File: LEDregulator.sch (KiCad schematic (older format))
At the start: 43 parts, among them J1 2.1mm DC jack, J2 2way Screw Terminal, J3 2way Screw Terminal, J4 2way Screw Terminal, J5 2way Screw Terminal, J6 2way Screw Terminal, J7 2way Screw Terminal, Q1 BSS138W, SW1 DPDT Switch, SW2 6pos rotary

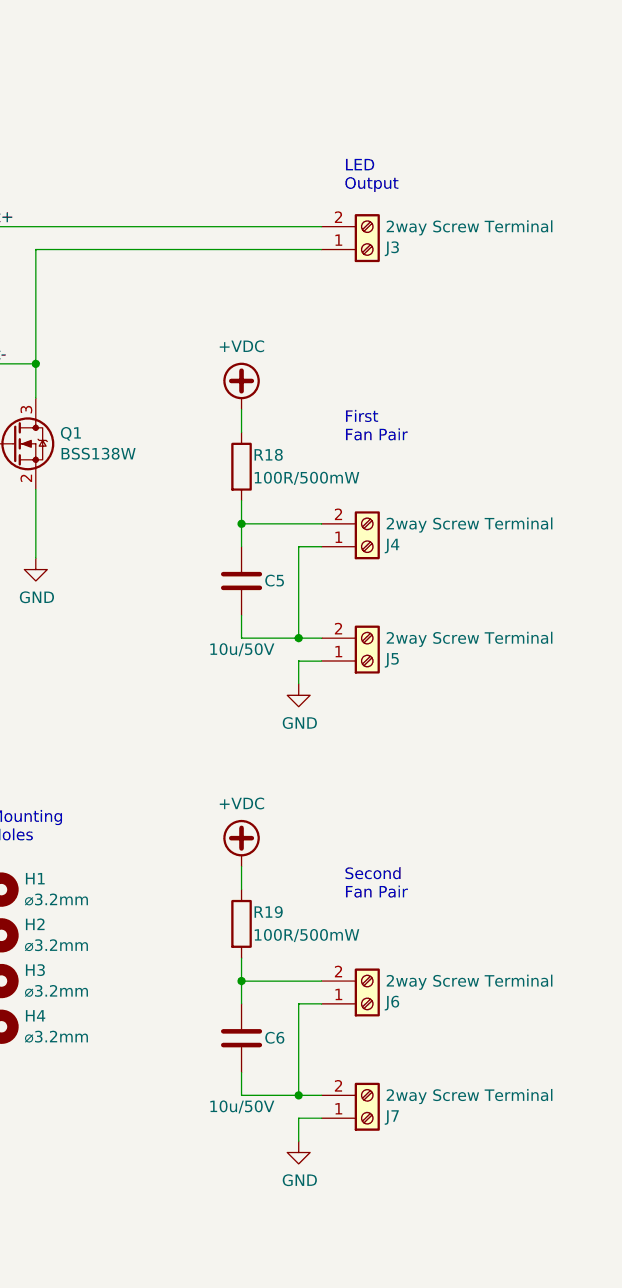
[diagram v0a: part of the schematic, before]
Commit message: Added labels for the types of fans and LED strips used. Changed the 3D package of the DC input connector.
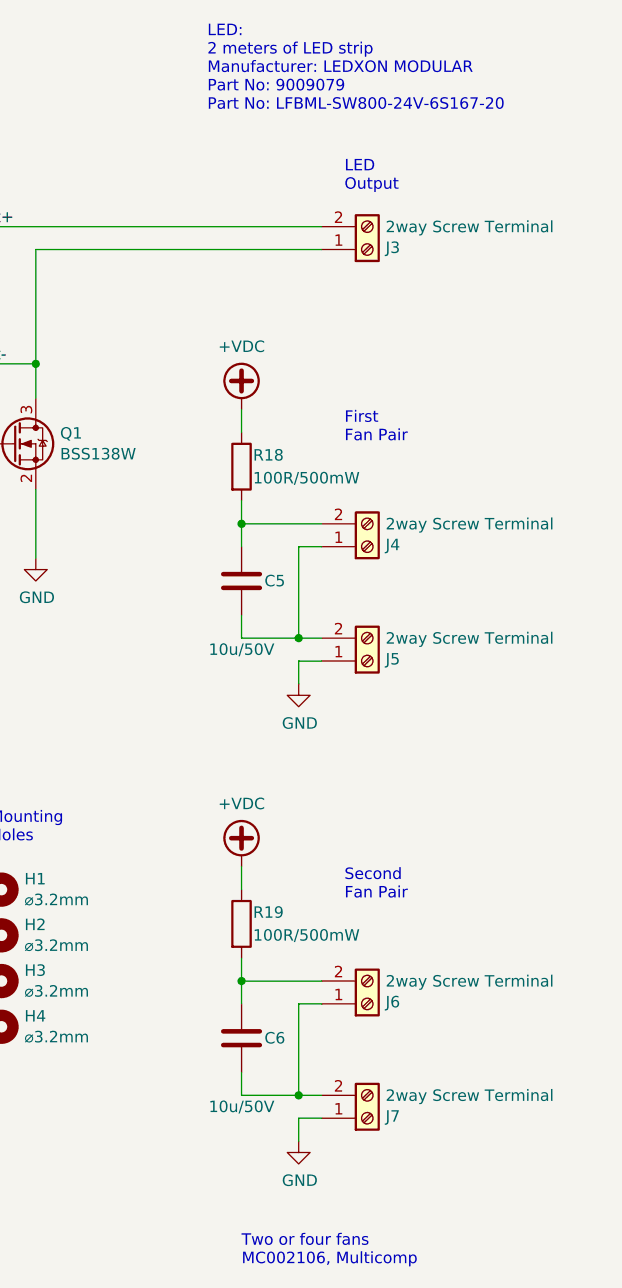
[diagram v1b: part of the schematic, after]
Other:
- note added: "LED:\n2 meters of LED strip\nManufacturer: LEDXON MODULAR \nPart No: 9009079 \nPart No: LFBML-SW800-24V-6S167-20"
- note added: "Two or four fans\nMC002106, Multicomp"
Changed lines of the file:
@@
 Wire Wire Line
 	2350 2350 2350 2250
+Text Notes 9650 6050 0    50   ~ 0
+Two or four fans\nMC002106, Multicomp
+Text Notes 9500 1000 0    50   ~ 0
+LED:\n2 meters of LED strip\nManufacturer: LEDXON MODULAR \nPart No: 9009079 \nPart No: LFBML-SW800-24V-6S167-20
 $EndSCHEMATC
